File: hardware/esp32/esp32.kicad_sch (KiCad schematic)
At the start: 47 parts, among them J1 Screw_Terminal_01x02, Q4 MMBT5401, Q5 MMBT2222A, U4 mini_esp32, U5 LMV321, U6 LMV321, U8 HT7533-1

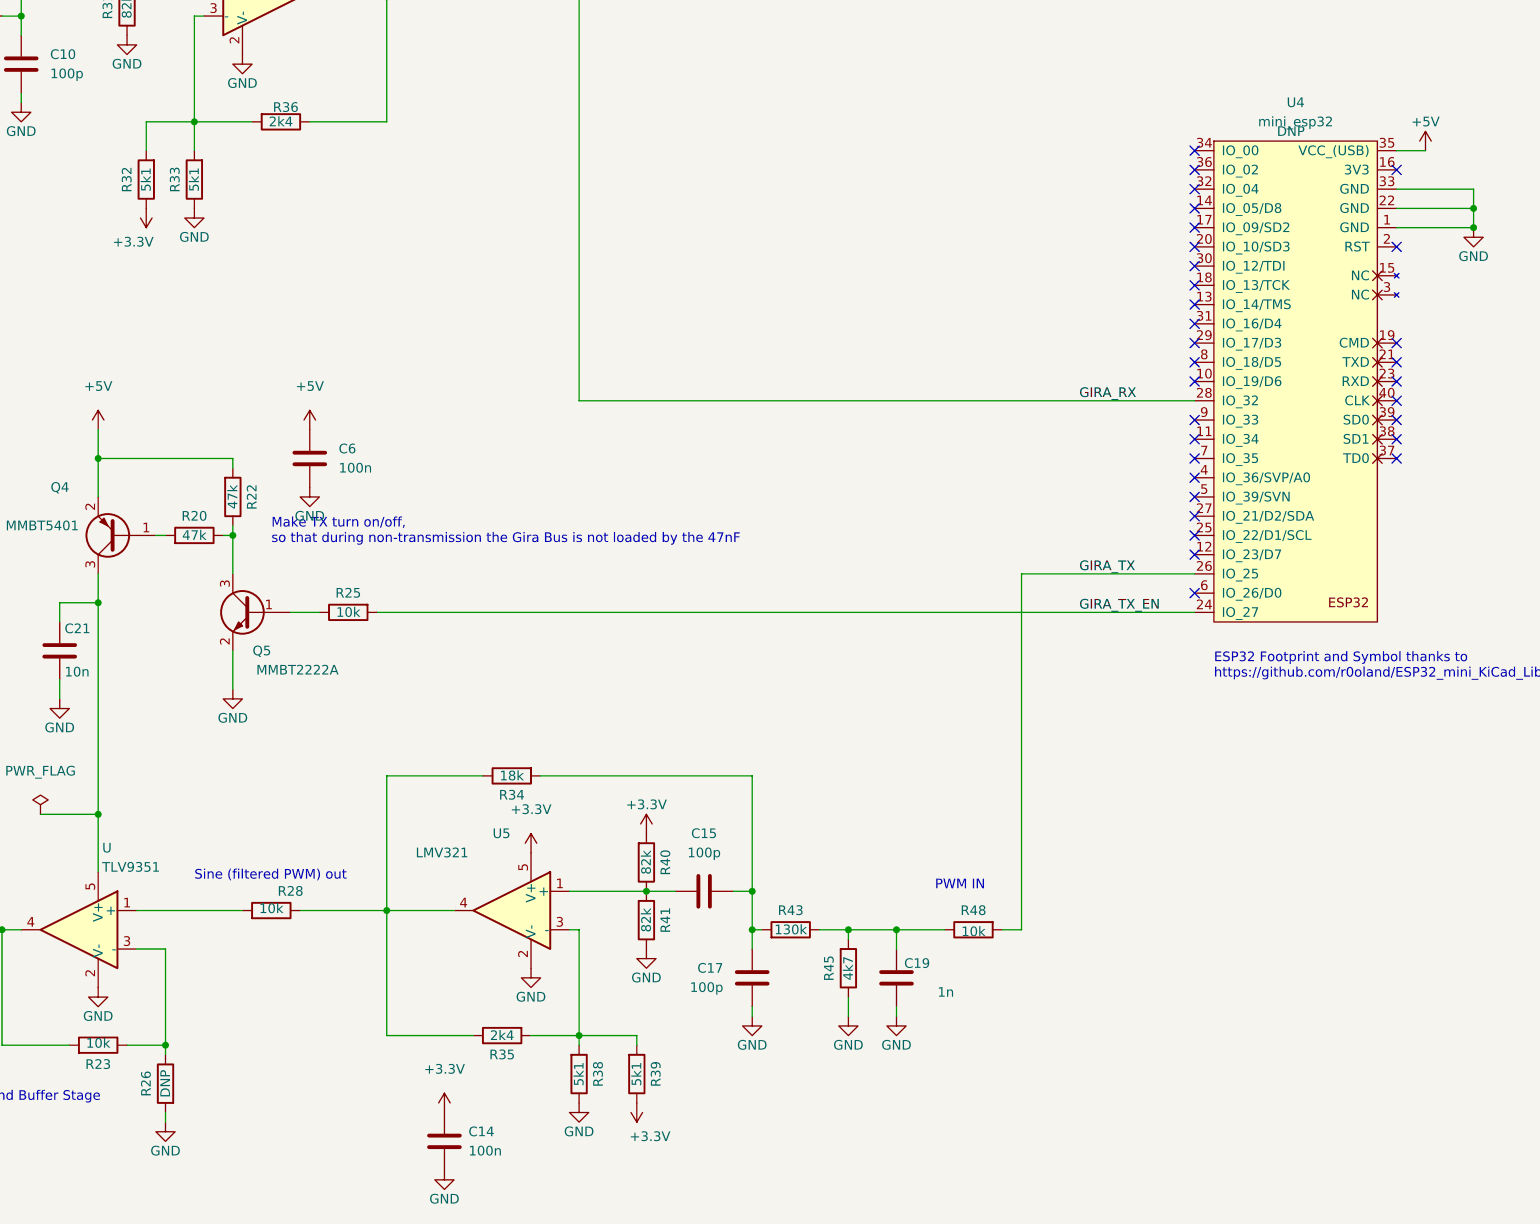
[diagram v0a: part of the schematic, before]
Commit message: Rough untested, uncompiled ESP32 firmware. Just transfer from stm32 code
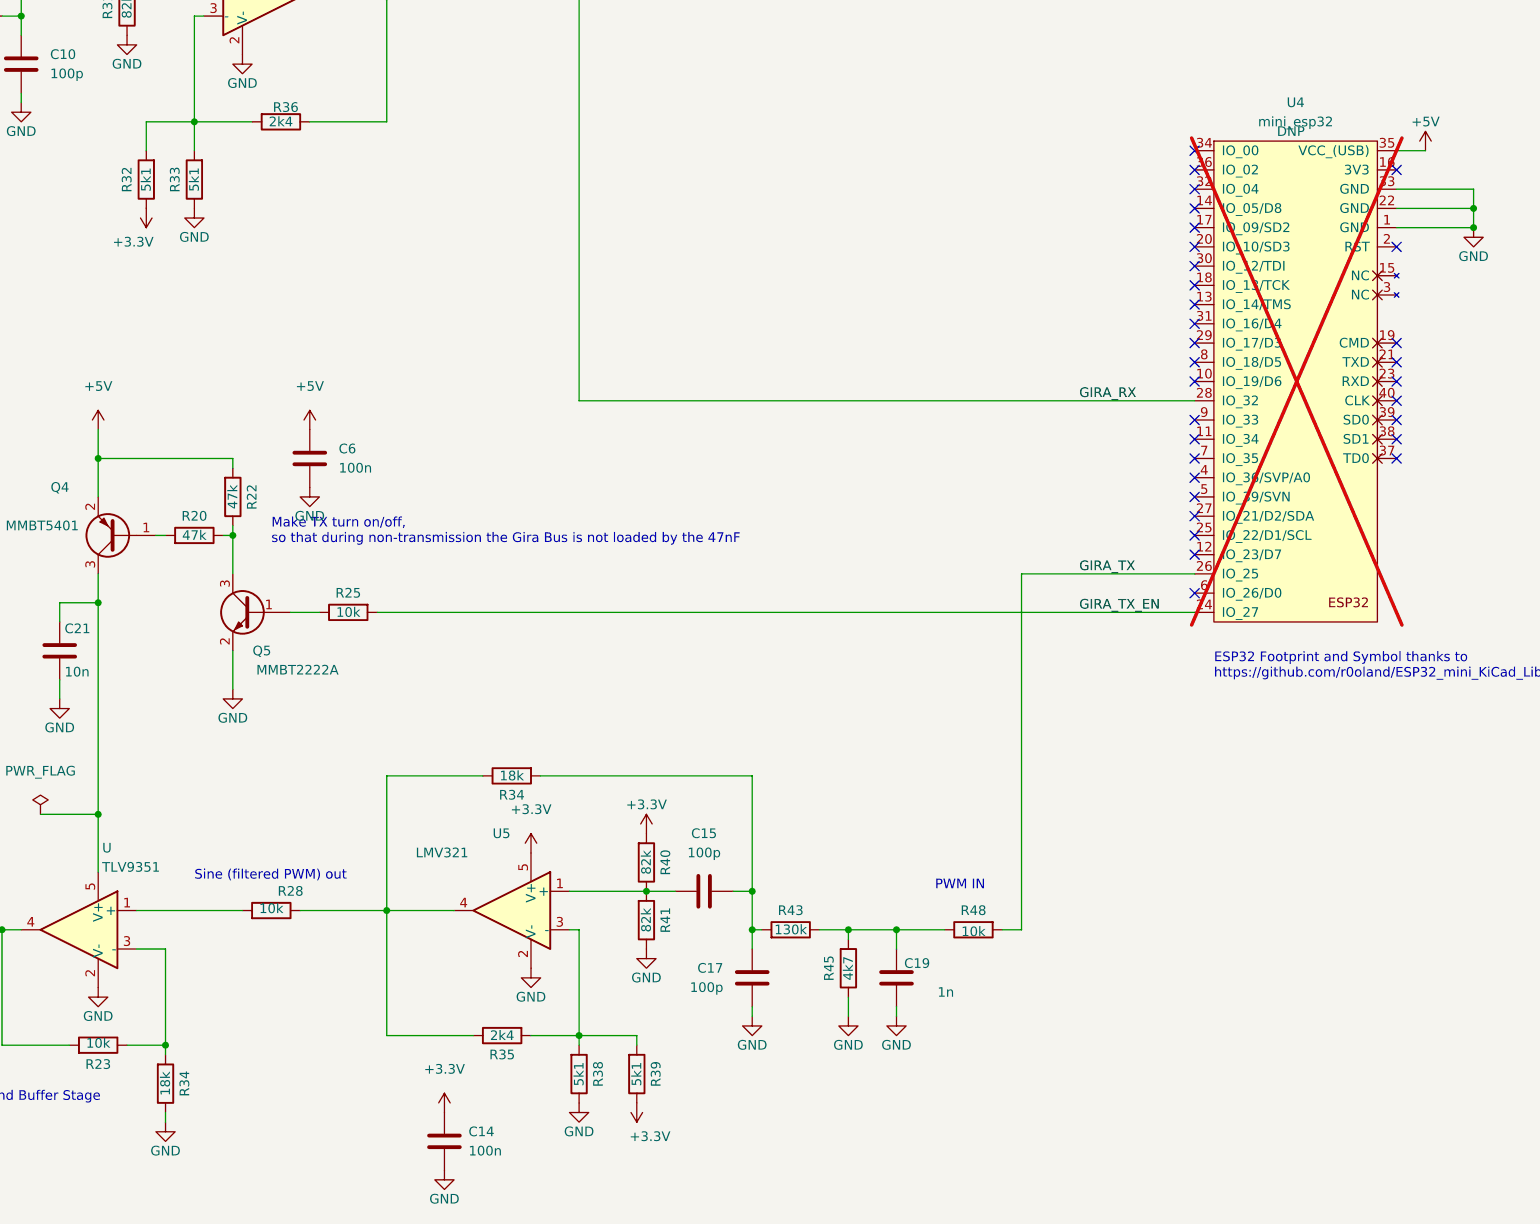
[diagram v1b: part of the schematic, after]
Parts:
- removed R26: DNP, Library:R_0603_1608Metric_Pad0.98x0.95mm_HandSolder, symbol symbols:RDNP
- added R34: 18k, Library:R_0603_1608Metric_Pad0.98x0.95mm_HandSolder, symbol symbols:18k
- U4: now not fitted
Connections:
- net GND: now also R34.1
- net at R23.1, U.3 (-): now also R34.2
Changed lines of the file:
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@@
-    )
-  )
-  (symbol (lib_id "symbols:RDNP") (at 149.86 196.85 0) (mirror y) (unit 1)
-    (in_bom yes) (on_board yes) (dnp no)
-    (property "Reference" "R26" (at 147.32 196.85 90)
-      (effects (font (size 1.27 1.27)))
-    )
-    (property "Value" "DNP" (at 149.86 196.85 90)
-      (effects (font (size 1.27 1.27)))
-    )
-    (property "Footprint" "Library:R_0603_1608Metric_Pad0.98x0.95mm_HandSolder" (at 151.638 196.85 90)
-      (effects (font (size 1.27 1.27)) hide)
-    )
-    (property "Datasheet" "~" (at 149.86 196.85 0)
-      (effects (font (size 1.27 1.27)) hide)
-    )
-    (property "MPN" "DNP" (at 149.86 196.85 0)
-      (effects (font (size 1.27 1.27)) hide)
-    )
-    (pin "1")
-    (pin "2")
-    (instances
-      (project "stm32"
-        (path "/60790c3a-d4fe-419d-bc96-3387cad42935"
-          (reference "R26") (unit 1)
-        )
-      )
-      (project "esp32"
-        (path "/a949f3be-99c7-4e8a-a2ba-844ff7c53a70"
-          (reference "R6") (unit 1)
-        )
-      )
     )
   )
@@
   )
   (symbol (lib_id "symbols:mini_esp32") (at 298.45 71.12 0) (unit 1)
-    (in_bom yes) (on_board yes) (dnp no) (fields_autoplaced)
+    (in_bom yes) (on_board yes) (dnp yes) (fields_autoplaced)
     (property "Reference" "U4" (at 299.085 67.31 0)
       (effects (font (size 1.27 1.27)))
@@
         )
       )
+    )
+  )
+  (symbol (lib_id "symbols:18k") (at 149.86 196.85 0) (mirror x) (unit 1)
+    (in_bom yes) (on_board yes) (dnp no)
+    (property "Reference" "R34" (at 152.4 196.85 90)
+      (effects (font (size 1.27 1.27)))
+    )
+    (property "Value" "18k" (at 149.86 196.85 90)
+      (effects (font (size 1.27 1.27)))
+    )
+    (property "Footprint" "Library:R_0603_1608Metric_Pad0.98x0.95mm_HandSolder" (at 148.082 196.85 90)
+      (effects (font (size 1.27 1.27)) hide)
+    )
+    (property "Datasheet" "~" (at 149.86 196.85 0)
+      (effects (font (size 1.27 1.27)) hide)
+    )
+    (property "MPN" "C25810" (at 149.86 196.85 0)
+      (effects (font (size 1.27 1.27)) hide)
+    )
+    (pin "1")
+    (pin "2")
+    (instances
+      (project "stm32"
+        (path "/60790c3a-d4fe-419d-bc96-3387cad42935"
+          (reference "R34") (unit 1)
+        )
+      )
+      (project "esp32"
+        (path "/a949f3be-99c7-4e8a-a2ba-844ff7c53a70"
+          (reference "R6") (unit 1)
+        )
+      )

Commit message: Start with next revision, which includes comparators
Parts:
- added C14: 100n, Library:C_0603_1608Metric_Pad1.08x0.95mm_HandSolder, symbol symbols:100n
- added R22 (x2): 47k, Library:R_0603_1608Metric_Pad0.98x0.95mm_HandSolder, symbol symbols:47k
- added R25 (x4): 10k, Library:R_0603_1608Metric_Pad0.98x0.95mm_HandSolder, symbol symbols:10k
- added R36 (x2): 2k4, Library:R_0603_1608Metric_Pad0.98x0.95mm_HandSolder, symbol symbols:2k4
- added R45 (x2): 4k7, Library:R_0603_1608Metric_Pad0.98x0.95mm_HandSolder, symbol symbols:4k7
- added unit 3 of U6
- added unit 2 of U6
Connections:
- net +3.3V: now also C14.1, R25.2, R25.2, R36.1, U6.8 (V+)
- net GIRA_RX: now also R45.2, R45.2
- net GND: now also C14.2, R25.1, U6.4 (V-)
- net GIRA_RX_DAC: now reaches U4.30 (IO_12/TDI)
- net GIRA_RX_DAC: now also R22.1, R25.1, U6.7
- net GIRA_RX_COMP: now reaches U4.32 (IO_04)
- net GIRA_RX_COMP: now also R22.1, R25.1, U6.1
- net GIRA_RX_THRES: now reaches U4.6 (IO_26/D0)
- net GIRA_RX_THRES: now also R36.2
- new net: R22.2, R36.1, U6.5 (+)
- new net: R45.1, U6.6 (-)
- new net: R45.1, U6.2 (-)
- new net: R22.2, R25.1, R25.2, U6.3 (+)
- new net: R25.2, R36.2
- no-connect marks 31 -> 28
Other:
- note added: "C7501280"
- note added: "V3.1 only"

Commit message: Work on V3.1
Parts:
- removed R20: 47k, Library:R_0603_1608Metric_Pad0.98x0.95mm_HandSolder, symbol symbols:47k
- removed R34: 18k, Library:R_0603_1608Metric_Pad0.98x0.95mm_HandSolder, symbol symbols:18k
- removed R48: 10k, Library:R_0603_1608Metric_Pad0.98x0.95mm_HandSolder, symbol symbols:10k
- removed U4: mini_esp32, Library:ESP32_mini, symbol symbols:mini_esp32
- added J2: ESP_left, Library:PinHeader_2x10_P2.54mm_Vertical, symbol symbols:ESP_left
- added J3: ESP_right, Library:PinHeader_2x10_P2.54mm_Vertical, symbol symbols:ESP_right
- added R22 (x2): 47k, Library:R_0603_1608Metric_Pad0.98x0.95mm_HandSolder, symbol symbols:47k
- added R25: 10k, Library:R_0603_1608Metric_Pad0.98x0.95mm_HandSolder, symbol symbols:10k
- added R45: 4k7, Library:R_0603_1608Metric_Pad0.98x0.95mm_HandSolder, symbol symbols:4k7
- R45: now not fitted
- U6: JlcRotOffset (none) -> -90
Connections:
- net +3.3V: no longer C14.1, R39.1, R40.2, U5.5 (V+)
- net +5V: now also C14.1, R39.1, R40.2, U5.5 (V+), J3.15 (VCC_(USB)), R22.2
- net GIRA_RX: now also J3.8 (IO_32)
- net GIRA_RX_COMP: now also J3.14 (IO_00)
- net GIRA_RX_DAC: now also J3.12 (IO_04)
- net GIRA_RX_THRES: now also J2.6 (IO_26/D0)
- net GIRA_TX: now also J3.6 (IO_25), R45.1
- net GIRA_TX_EN: now also J3.4 (IO_27)
- net GND: now also J2.1 (GND), J3.13 (GND), J3.2 (GND), R22.2
- net at C19.2, R43.1, R45.2: now also R45.2
- net at Q5.3 (C), R22.1: now also R25.2
- net at Q4.1 (B1): now also R25.1
- net at R23.1, U.3 (-): now also R22.1, R22.1
- no-connect marks 28 -> 30
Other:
- note removed: "C7501280"
- moved on the sheet: C10, C12, C14, C15, C16, C17, C19, C21, C4, C6, D1, Q4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
